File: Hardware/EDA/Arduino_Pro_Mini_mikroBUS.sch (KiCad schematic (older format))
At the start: 34 parts, among them J1 HEADER_F_2.54MM_1R8P_ST_AU_PTH, J2 HEADER_F_2.54MM_1R8P_ST_AU_PTH, J3 HEADER_F_2.54MM_1R12P_ST_AU_P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, J4 HEADER_F_2.54MM_1R12P_ST_AU_P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, J5 Molex_0475710001, J6 HEADER_F_2.54MM_1R2P_ST_AU_PTH, M1 FID, M2 FID, M3 FID, P1 HEADER_M_2.54MM_1R3P_ST_AU_PTH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

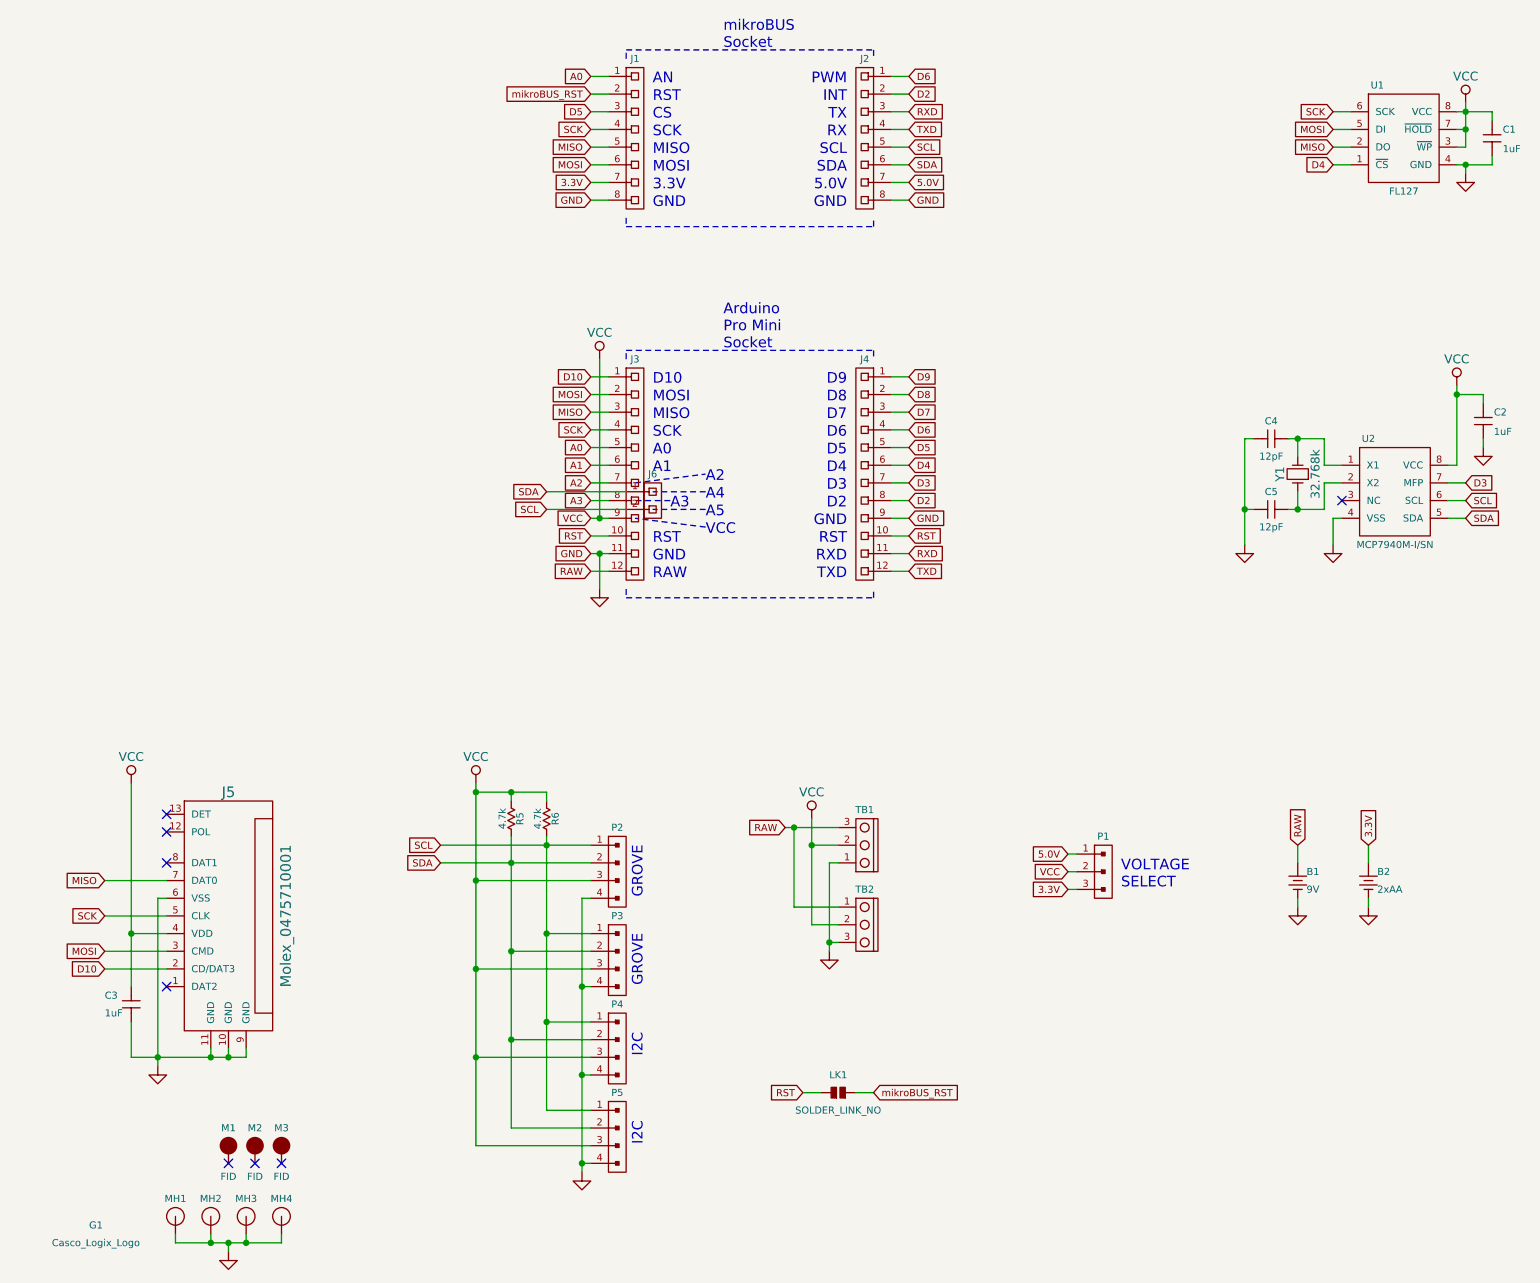
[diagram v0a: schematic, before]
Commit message: Added layout for RTC crystal and caps. Re-routed several traces as-needed. Updated RTC and crystal component parameters in schematic and regenerated netlist. Gerbers generated - need final review before release.
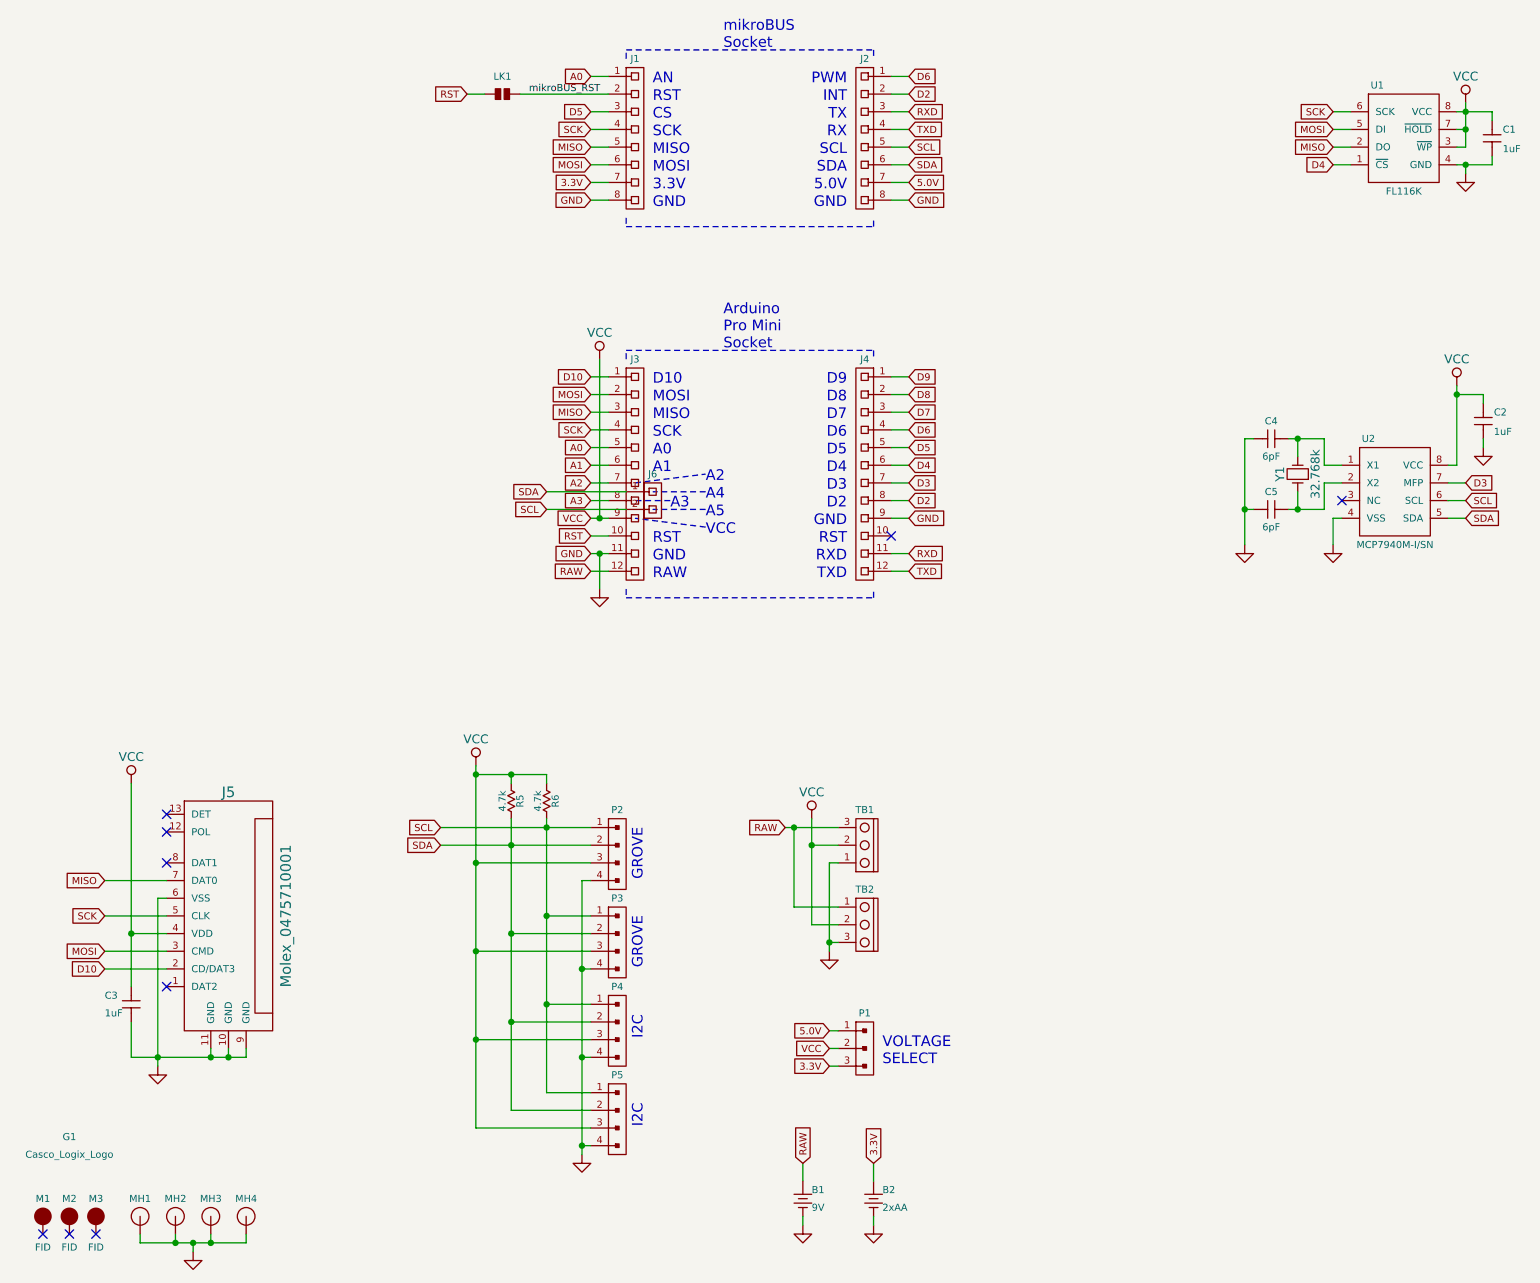
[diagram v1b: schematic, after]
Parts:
- C4, C5: value 12pF -> 6pF; Manufacturer (none) -> Mfr; Manufacturer P/N (none) -> Mfr P/N; Supplier (none) -> Supplier; Supplier P/N (none) -> Supplier P/N
- U1: value FL127 -> FL116K
- U2: Manufacturer (none) -> Microchip; Supplier (none) -> Digi-Key
- Y1: Manufacturer (none) -> Abracon; Manufacturer P/N (none) -> ABS07-120-32.768KHZ-T; Supplier (none) -> Supplier; Supplier P/N (none) -> 535-11937-1-ND
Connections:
- net RST: no longer J4.10 (P1)
- no-connect marks 8 -> 9
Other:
- moved on the sheet: B1, B2, LK1, M1, M2, M3, MH1, MH2, MH3, MH4, P1, P2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

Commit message: Updated date in schematic and PCB title block. Regenerated PDF schematic. Verified gerbers.
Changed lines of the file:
@@
 Sheet 1 1
 Title "Arduino Pro Mini mikroBUS Develepment Board"
-Date "2018-02-11"
+Date "2018-04-07"
 Rev "1.1"
 Comp "Casco Logix, LLC"
@@
 08 2C 10 08 2A 2D 42 01 0A 04 82 4A 8B 50 80 02 81 A0 D2 22 14 A0 40 20 A8 B4 08 05 28 10 08 2A
 2D 42 01 0A 04 82 4A 8B AA 99 BB 25 10 08 04 02 37 21 7A 80 02 81 A0 D2 F2 FF 6C 4F 00 04 F4 D6
-7A A4 00 00 00 00 49 45 4E 44 AE 42 60 82 9D
+7A A4 00 00 00 00 49 45 4E 44 AE 42 60 82 8E
 EndData
 $EndBitmap
@@
 	8150 3500 8050 3500
 Wire Wire Line
-	8050 3650 8050 3500
-Wire Wire Line
-	7850 3650 8050 3650
+	8050 3500 8050 3650
+Wire Wire Line
+	8050 3650 7850 3650
 Wire Wire Line
 	7900 3650 7900 3550
